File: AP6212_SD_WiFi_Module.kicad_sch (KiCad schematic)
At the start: 21 parts, among them J1 Conn_Coaxial, J2 TF_Card, U1 AP6212, Y1 26MHz

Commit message: feat: Change the crystal package to SMD 3225
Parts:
- Y1: footprint Crystal:Crystal_SMD_0603-4Pin_6.0x3.5mm -> Crystal:Crystal_SMD_3225-4Pin_3.2x2.5mm
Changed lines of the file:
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@@
       (effects (font (size 1.27 1.27)))
     )
-    (property "Footprint" "Crystal:Crystal_SMD_0603-4Pin_6.0x3.5mm" (at 110.49 153.67 0)
+    (property "Footprint" "Crystal:Crystal_SMD_3225-4Pin_3.2x2.5mm" (at 110.49 153.67 0)
       (effects (font (size 1.27 1.27)) hide)
     )

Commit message: feat: Optimized antenna layout and routing
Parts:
- removed L2, L3: 3.3nH, Inductor_SMD:L_0402_1005Metric, symbol Device:L_Small
- added C3, C4: 3.3nH, Capacitor_SMD:C_0402_1005Metric, symbol Device:C_Small
- added C5: DNP, Capacitor_SMD:C_0402_1005Metric, symbol Device:C
- renumbered C3 to C6, C4 to C7, C5 to C8, C6 to C9, L4 to L2
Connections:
- net GND: now also C3.2, C4.2, C5.1
- net at J1.1 (In), L1.1, U1.2 (WL_BT_ANT): now also C4.1, C5.2
- net at AE1.1 (A), L1.2: now also C3.1

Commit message: feat: Replace 4.7uH inductor package to VLS252012
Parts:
- L2: footprint Inductor_SMD:L_TDK_NLV25_2.5x2.0mm -> Custom_Libs:IND-SMD_L2.5-W2.0_VLS2520X
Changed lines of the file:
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@@
       (effects (font (size 1.27 1.27)) (justify left))
     )
-    (property "Footprint" "Inductor_SMD:L_TDK_NLV25_2.5x2.0mm" (at 182.88 189.23 0)
+    (property "Footprint" "Custom_Libs:IND-SMD_L2.5-W2.0_VLS2520X" (at 182.88 189.23 0)
       (effects (font (size 1.27 1.27)) hide)
     )

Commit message: feat: Replace 4.7uH inductor package to SWPA252012
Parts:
- L2: footprint Custom_Libs:IND-SMD_L2.5-W2.0_VLS2520X -> Custom_Libs:IND-SMD_L2.5-W2.0
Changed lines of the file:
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@@
       (effects (font (size 1.27 1.27)) (justify left))
     )
-    (property "Footprint" "Custom_Libs:IND-SMD_L2.5-W2.0_VLS2520X" (at 182.88 189.23 0)
+    (property "Footprint" "Custom_Libs:IND-SMD_L2.5-W2.0" (at 182.88 189.23 0)
       (effects (font (size 1.27 1.27)) hide)
     )

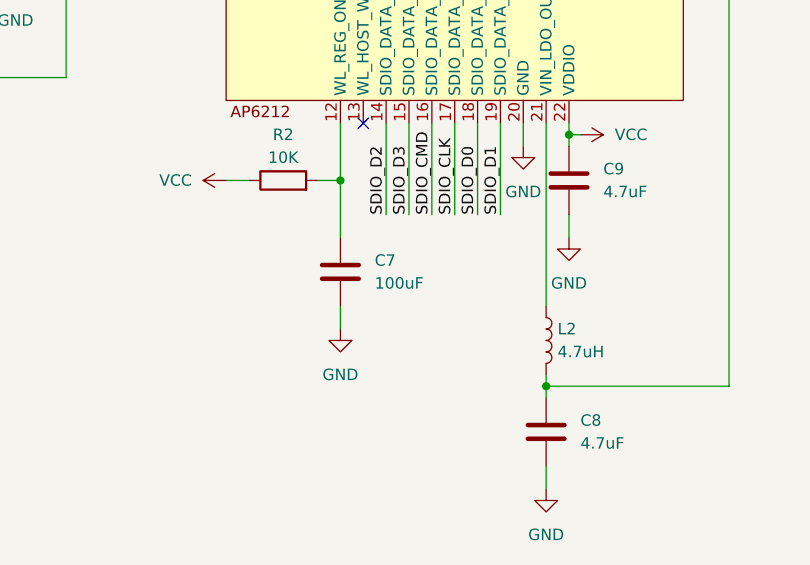
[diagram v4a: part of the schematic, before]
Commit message: feat: Modify the C7 parameter value of 0.1 uF
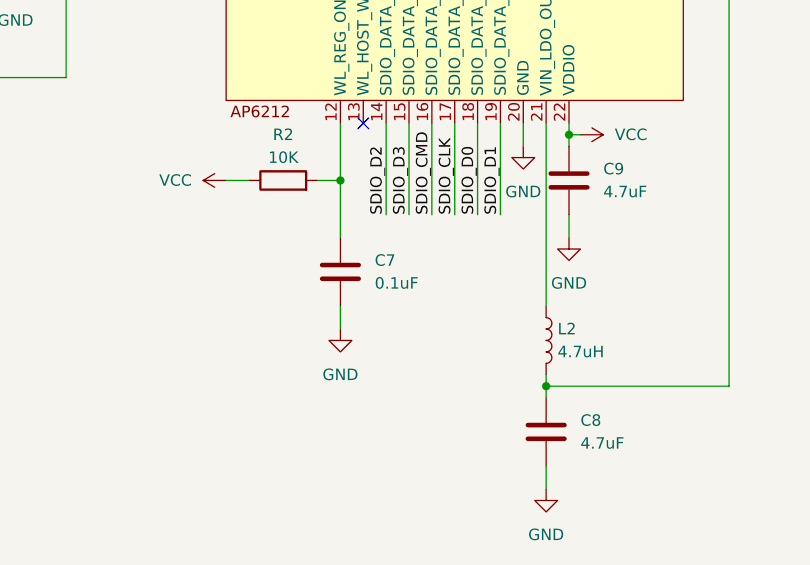
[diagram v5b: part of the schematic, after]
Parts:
- C7: value 100uF -> 0.1uF
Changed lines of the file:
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@@
       (effects (font (size 1.27 1.27)) (justify left))
     )
-    (property "Value" "100uF" (at 163.83 182.88 0)
+    (property "Value" "0.1uF" (at 163.83 182.88 0)
       (effects (font (size 1.27 1.27)) (justify left))
     )

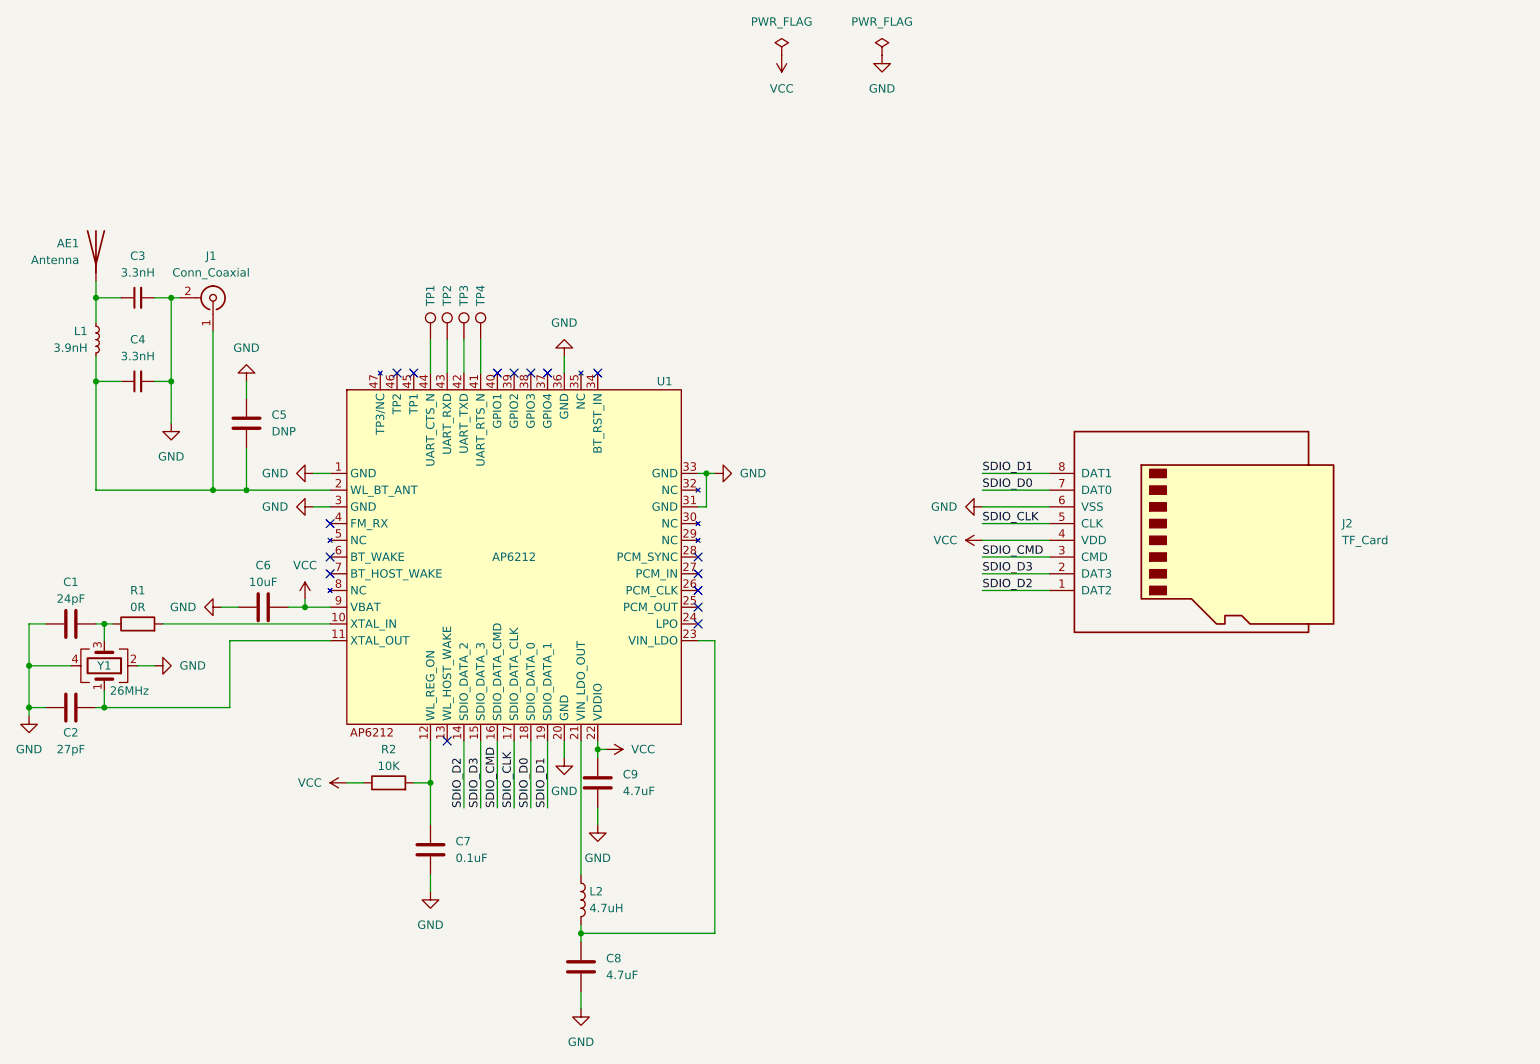
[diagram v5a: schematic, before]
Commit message: feat: Removed the test point and completed the LPO part of the peripheral circuit
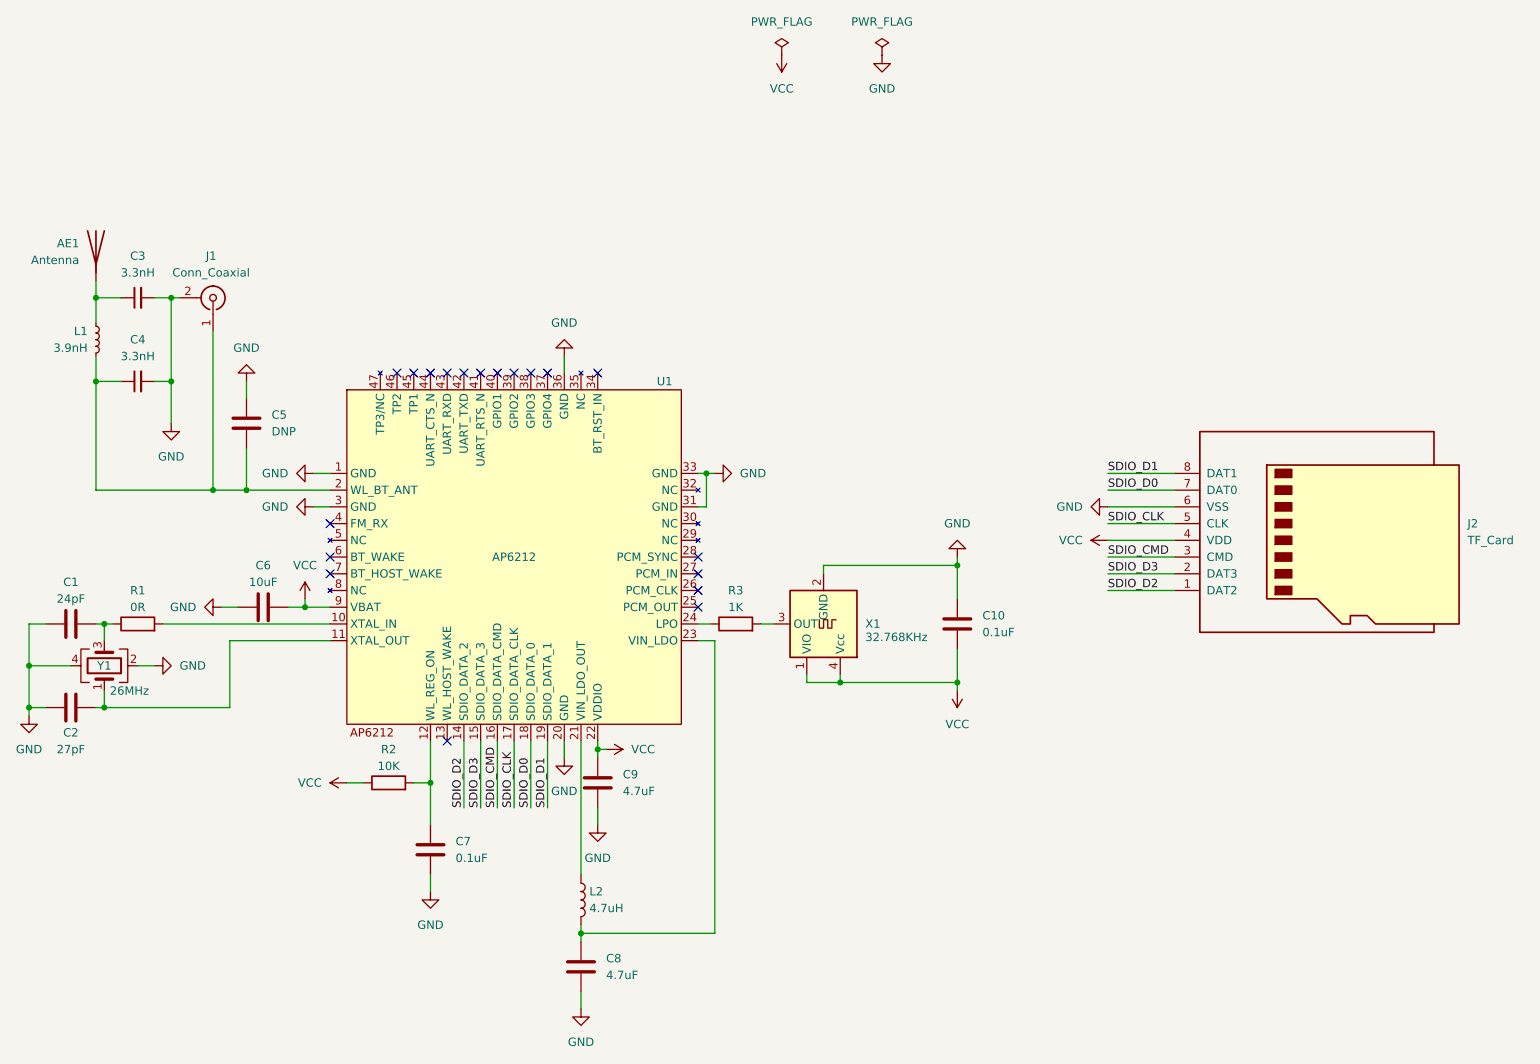
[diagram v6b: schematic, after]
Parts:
- removed TP1: CTS, TestPoint:TestPoint_Pad_D1.0mm, symbol Connector:TestPoint
- removed TP2: RXD, TestPoint:TestPoint_Pad_D1.0mm, symbol Connector:TestPoint
- removed TP3: TXD, TestPoint:TestPoint_Pad_D1.0mm, symbol Connector:TestPoint
- removed TP4: RTS, TestPoint:TestPoint_Pad_D1.0mm, symbol Connector:TestPoint
- added C10: 0.1uF, Capacitor_SMD:C_0603_1608Metric, symbol Device:C
- added R3: 1K, Resistor_SMD:R_0603_1608Metric, symbol Device:R
- added X1: 32.768KHz, Crystal:Crystal_SMD_3225-4Pin_3.2x2.5mm, symbol Oscillator:SG-3030CM
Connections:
- net GND: now also C10.1, X1.2 (GND)
- net VCC: now also C10.2, X1.1 (VIO), X1.4 (Vcc)
- net at U1.24 (LPO): now also R3.1
- new net: R3.2, X1.3 (OUT)
- no-connect marks 16 -> 19
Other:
- moved on the sheet: J2
